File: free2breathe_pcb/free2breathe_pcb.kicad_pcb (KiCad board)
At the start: 2 copper layers, 108.5 x 115 mm, 102 parts, among them J1 USB4110-GF-A_REVB, J2 LED_Connector, J3 Alarm_Connector, Q1 AO3401A, Q2 DMN3404L, U1 IP5328, U2 MCP6044-E/P, U3 MCP6044-E/P, U4 SO2 Sensor, U5 CO Sensor, U6 MCP6044-E/P, U7 O3 Sensor, U8 MCP6044-E/P, U9 NO2 Sensor

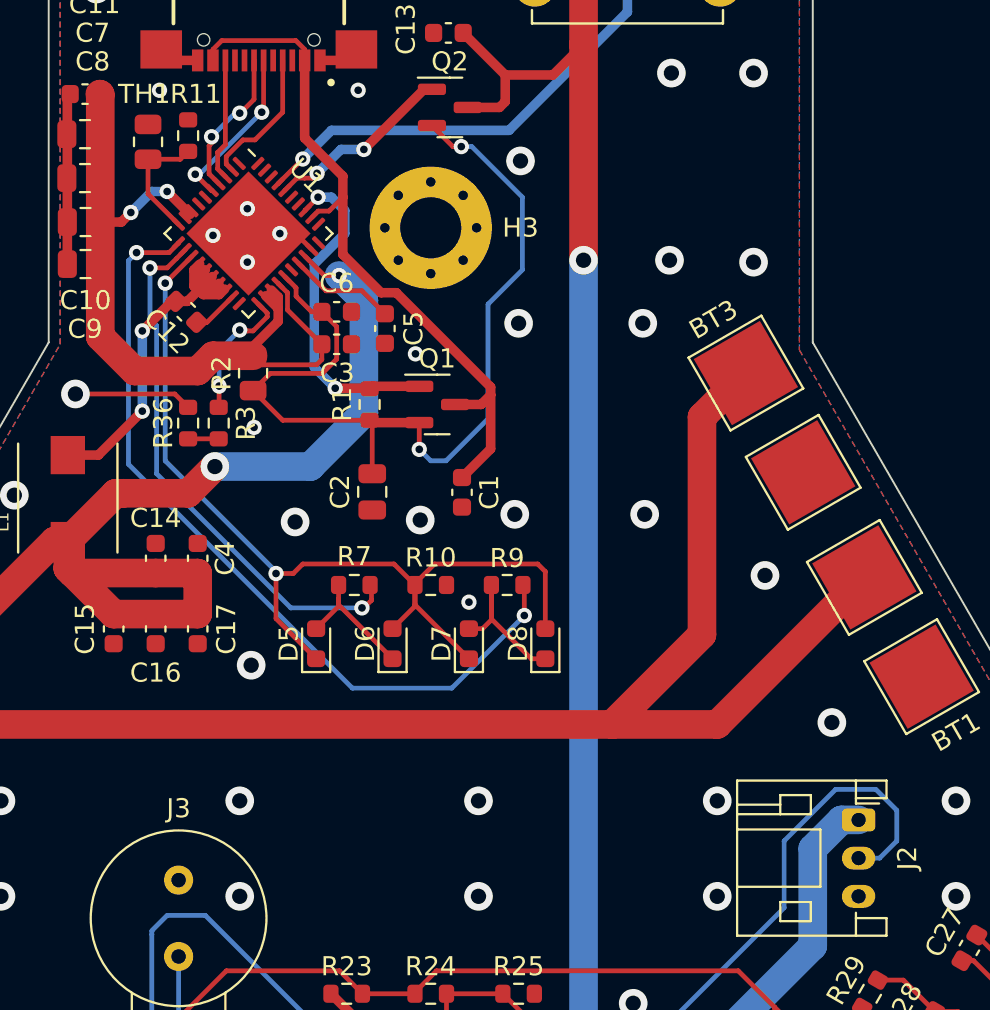
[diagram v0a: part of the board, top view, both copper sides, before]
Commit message: add fabrication files, update todo
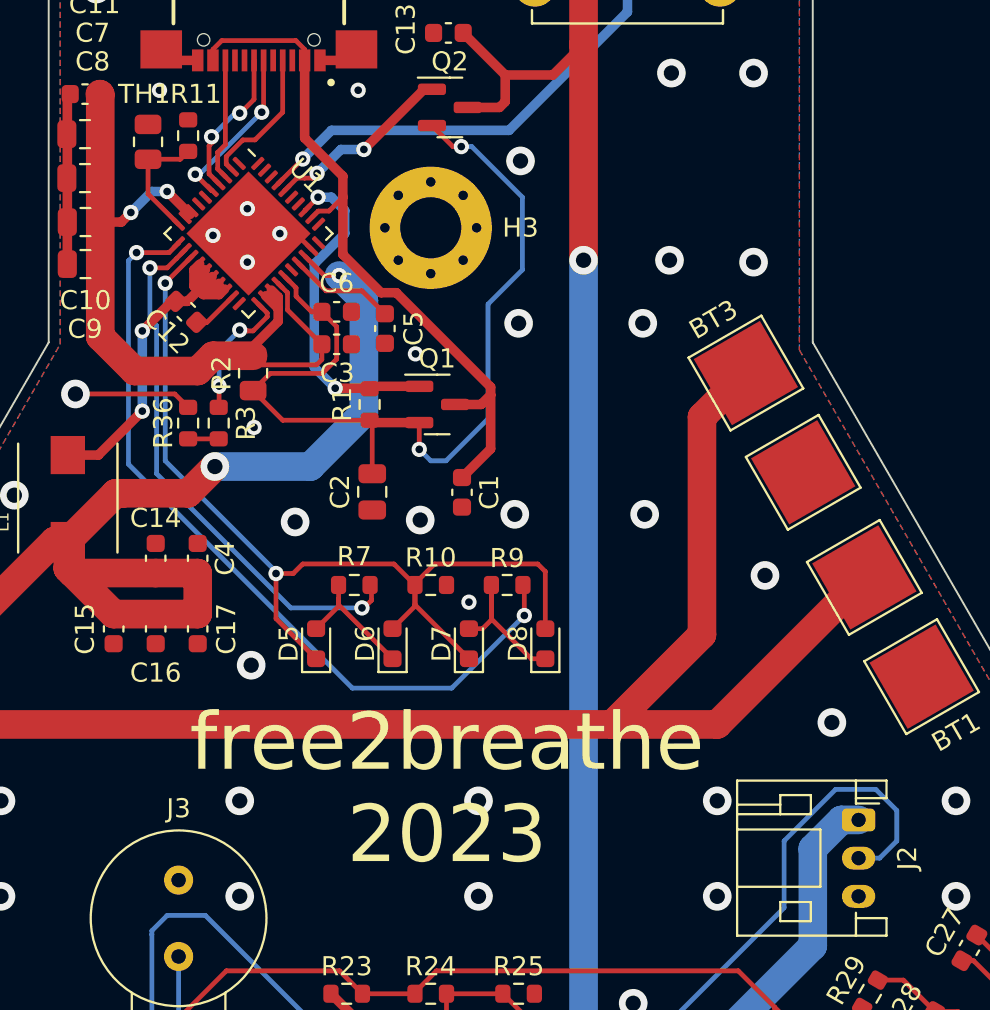
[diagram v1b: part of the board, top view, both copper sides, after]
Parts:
- added G***: LOGO, LOGO, B.Cu at (121.7, 92.5)
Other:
- board text added: "free2breathe 2023"

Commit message: start layout v2
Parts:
- added C33: 0.1u, Capacitor_SMD:C_0603_1608Metric, F.Cu at (196.1, 133.9)
- added R37: 49.9, Resistor_SMD:R_0603_1608Metric, F.Cu at (67.4, 161.8)
- added R38: 49.9, Resistor_SMD:R_0603_1608Metric, F.Cu at (190.3, 131.8)
- added R39: 100k, Resistor_SMD:R_0603_1608Metric, F.Cu at (81.4, 168.4)
- added R40: 499k, Resistor_SMD:R_0603_1608Metric, F.Cu at (193.1, 127.7)
- C15: value 22uF 16v -> 22uF 16V
- C18, C19, C24, C25: value 0.1u -> 1u
- R12: value 10 -> 2k
- R13: value 10k -> 1M
- R14, R16, R20, R21, R26, R28, R29, R31, R34, R35: value 10 -> 1M
- R15, R30: value 10 -> 16.2k
- R17: value 4.7k -> 1M
- R18, R19, R32, R33: value 10 -> 100K
- R22: value 10 -> 49.9
- R23: value 10k -> 49.9
- R24: value 910 -> 100k
- R25: value 4.7k -> 499k
- R27: value 10 -> 143k
- U4: value SO2 Sensor -> O3 Sensor
- U7: value O3 Sensor -> MCP6044-E/P; footprint components:XDCR_110-102 -> components:DIP254P762X533-14
- U8: value MCP6044-E/P -> SO2 Sensor; footprint components:DIP254P762X533-14 -> components:XDCR_110-102
- moved R19 107.4 mm to (183.7, 158.2), turned to 0 degrees
- moved C21 99.4 mm to (180.2, 163.9), turned to 0 degrees
- moved C28 98.0 mm to (67.6, 165.4), turned to 0 degrees
- moved R21 96.4 mm to (171.0, 159.8), turned to 0 degrees
- moved C23 95.9 mm to (166.5, 163.0), turned to 0 degrees
- moved R16 91.1 mm to (170.2, 155.9), turned to 0 degrees
- moved R27 90.1 mm to (73.8, 155.2), turned to 0 degrees
- moved R34 86.6 mm to (65.5, 157.8), turned to 0 degrees
- moved R23 83.4 mm to (173.8, 164.8)
- moved R14 79.7 mm to (162.7, 160.9), turned to 0 degrees
- moved R26 77.9 mm to (73.1, 151.4), turned to 0 degrees
- moved R25 75.8 mm to (178.0, 158.9)
- moved C24 74.7 mm to (175.3, 156.3), turned to 0 degrees
- moved C31 74.0 mm to (68.0, 110.1), turned to 0 degrees
- moved C26 73.2 mm to (72.2, 169.2), turned to 0 degrees
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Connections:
- A1 pad 23: /Arduino_A4 -> unconnected-(A1-Pad23)
- A1 pad 24: /Arduino_A5 -> unconnected-(A1-Pad24)
- A1 pad 25: /Arduino_A6 -> unconnected-(A1-Pad25)
- A1 pad 26: /Arduino_A7 -> unconnected-(A1-Pad26)
- C18 pad 1: Net-(C18-Pad1) -> Net-(R34-Pad2)
- C18 pad 2: Net-(C18-Pad2) -> GND
- C19 pad 1: Net-(C19-Pad1) -> Net-(R20-Pad2)
- C19 pad 2: Net-(C19-Pad2) -> GND
- C20 pad 2: GND -> Net-(C20-Pad2)
- C21 pad 2: GND -> Net-(C21-Pad2)
- C24 pad 1: Net-(C24-Pad1) -> Net-(R21-Pad2)
- C25 pad 1: Net-(C25-Pad1) -> Net-(R35-Pad2)
- C25 pad 2: Net-(C25-Pad2) -> GND
- C26 pad 2: GND -> Net-(C26-Pad2)
- C28 pad 2: GND -> Net-(C28-Pad2)
- C30 pad 1: Net-(C30-Pad1) -> Net-(R32-Pad2)
- C31 pad 1: Net-(C31-Pad1) -> Net-(R18-Pad2)
- C31 pad 2: Net-(C31-Pad2) -> GND
- C32 pad 1: Net-(C32-Pad1) -> Net-(R19-Pad2)
- R12 pad 1: Net-(C18-Pad1) -> Net-(R12-Pad1)
- R13 pad 2: /1.024V -> Net-(R12-Pad1)
- R14 pad 1: Net-(C19-Pad1) -> /Arduino_3V3
- R15 pad 1: /Divider_Low -> Net-(R14-Pad2)
- R15 pad 2: Net-(C20-Pad1) -> Net-(R15-Pad2)
- R16 pad 1: /1.024V -> Net-(R15-Pad2)
- R16 pad 2: Net-(C21-Pad1) -> GND
- R17 pad 1: /1.024V -> Net-(R12-Pad2)
- R18 pad 1: Net-(R18-Pad1) -> Net-(C20-Pad2)
- R18 pad 2: Net-(C22-Pad2) -> Net-(R18-Pad2)
- R19 pad 1: Net-(R19-Pad1) -> Net-(C21-Pad2)
- R19 pad 2: Net-(C23-Pad2) -> Net-(R19-Pad2)
- R20 pad 1: Net-(C22-Pad2) -> Net-(R20-Pad1)
- R20 pad 2: Net-(C22-Pad1) -> Net-(R20-Pad2)
- R21 pad 1: Net-(C23-Pad2) -> Net-(R21-Pad1)
- R21 pad 2: Net-(C23-Pad1) -> Net-(R21-Pad2)
- R22 pad 1: /Divider_High -> Net-(R22-Pad1)
- R22 pad 2: Net-(C24-Pad1) -> Net-(C22-Pad2)
- R23 pad 1: /Arduino_3V3 -> Net-(R23-Pad1)
- R23 pad 2: /Divider_High -> Net-(C23-Pad2)
- R24 pad 1: /Divider_High -> Net-(C20-Pad2)
- R24 pad 2: /Divider_Low -> Net-(C20-Pad1)
- R25 pad 1: /Divider_Low -> Net-(C21-Pad2)
- R25 pad 2: GND -> Net-(C21-Pad1)
- R26 pad 1: Net-(C25-Pad1) -> /Arduino_3V3
- R27 pad 1: Net-(C27-Pad1) -> Net-(R26-Pad2)
- R28 pad 1: /Divider_High -> Net-(R27-Pad2)
- R28 pad 2: Net-(C26-Pad1) -> GND
- R29 pad 1: /Divider_High -> /Arduino_3V3
- R29 pad 2: Net-(C28-Pad1) -> Net-(R29-Pad2)
- R30 pad 1: Net-(R30-Pad1) -> Net-(R29-Pad2)
- R30 pad 2: Net-(C29-Pad2) -> Net-(R30-Pad2)
- R31 pad 1: Net-(R31-Pad1) -> Net-(R30-Pad2)
- R31 pad 2: Net-(C31-Pad2) -> GND
- R32 pad 1: Net-(C29-Pad2) -> Net-(C26-Pad2)
- R32 pad 2: Net-(C29-Pad1) -> Net-(R32-Pad2)
- R33 pad 1: /Divider_Low -> Net-(C27-Pad2)
- R33 pad 2: Net-(C30-Pad1) -> Net-(R33-Pad2)
- R34 pad 1: Net-(C31-Pad2) -> Net-(R34-Pad1)
- R34 pad 2: Net-(C31-Pad1) -> Net-(R34-Pad2)
- R35 pad 1: /Divider_Low -> Net-(R35-Pad1)
- R35 pad 2: Net-(C32-Pad1) -> Net-(R35-Pad2)
- U2 pad 1: Net-(C18-Pad1) -> Net-(R21-Pad1)
- U2 pad 10: Net-(C22-Pad2) -> Net-(R14-Pad2)
- U2 pad 12: Net-(C22-Pad1) -> Net-(R19-Pad2)
- U2 pad 2: Net-(C18-Pad2) -> Net-(C23-Pad1)
- U2 pad 3: Net-(C20-Pad1) -> Net-(R15-Pad2)
- U2 pad 5: Net-(C24-Pad1) -> Net-(R21-Pad2)
- U2 pad 6: Net-(C22-Pad2) -> Net-(R23-Pad1)
- U2 pad 7: Net-(C22-Pad1) -> Net-(R23-Pad1)
- U2 pad 8: /Arduino_A3 -> Net-(C21-Pad2)
- U2 pad 9: /Arduino_A3 -> Net-(C21-Pad1)
- U3 pad 1: Net-(C19-Pad1) -> Net-(R20-Pad1)
- U3 pad 10: Net-(C23-Pad2) -> Net-(R12-Pad2)
- U3 pad 12: Net-(C23-Pad1) -> Net-(R18-Pad2)
- U3 pad 2: Net-(C19-Pad2) -> Net-(C22-Pad1)
- U3 pad 3: Net-(C21-Pad1) -> Net-(R12-Pad1)
- U3 pad 5: Net-(C21-Pad1) -> Net-(R20-Pad2)
- U3 pad 6: Net-(C23-Pad2) -> Net-(R22-Pad1)
- U3 pad 7: Net-(C23-Pad1) -> Net-(R22-Pad1)
- U3 pad 8: /Arduino_A1 -> Net-(C20-Pad2)
- U3 pad 9: /Arduino_A1 -> Net-(C20-Pad1)
- U4 pad 1: Net-(R18-Pad1) -> Net-(C21-Pad1)
- U4 pad 4: Net-(C18-Pad2) -> Net-(C23-Pad1)
- U4 pad 5: Net-(R12-Pad2) -> Net-(C23-Pad2)
- U4 pad 6: Net-(R18-Pad1) -> Net-(C21-Pad1)
- U5 pad 1: Net-(R19-Pad1) -> Net-(C20-Pad1)
- U5 pad 4: Net-(C19-Pad2) -> Net-(C22-Pad1)
- U5 pad 5: Net-(R14-Pad2) -> Net-(C22-Pad2)
- U5 pad 6: Net-(R19-Pad1) -> Net-(C20-Pad1)
- U6 pad 1: Net-(C25-Pad1) -> Net-(R34-Pad1)
- U6 pad 10: Net-(C29-Pad2) -> Net-(R27-Pad2)
- U6 pad 12: Net-(C29-Pad1) -> Net-(R32-Pad2)
- U6 pad 13: /Arduino_A4 -> /Arduino_A1
- U6 pad 14: /Arduino_A4 -> /Arduino_A1
- U6 pad 2: Net-(C25-Pad2) -> Net-(C28-Pad1)
- U6 pad 3: Net-(C26-Pad1) -> Net-(R26-Pad2)
- U6 pad 5: Net-(C30-Pad1) -> Net-(R34-Pad2)
- U6 pad 6: Net-(C29-Pad2) -> Net-(R37-Pad1)
- U6 pad 7: Net-(C29-Pad1) -> Net-(R37-Pad1)
- U6 pad 8: /Arduino_A5 -> Net-(C26-Pad2)
- U6 pad 9: /Arduino_A5 -> Net-(C26-Pad1)
- U7 pad 1: Net-(R30-Pad1) -> Net-(R35-Pad1)
- U7 pad 2: unconnected-(U7-Pad2) -> Net-(C29-Pad1)
- U7 pad 3: unconnected-(U7-Pad3) -> Net-(R30-Pad2)
- U7 pad 4: Net-(C25-Pad2) -> /Arduino_3V3
- U7 pad 5: Net-(R26-Pad2) -> Net-(R35-Pad2)
- U7 pad 6: Net-(R30-Pad1) -> Net-(R38-Pad1)
- U8 pad 1: Net-(C27-Pad1) -> Net-(C26-Pad1)
- U8 pad 2: Net-(C27-Pad2) -> unconnected-(U8-Pad2)
- U8 pad 3: Net-(C28-Pad1) -> unconnected-(U8-Pad3)
- U8 pad 4: /Arduino_3V3 -> Net-(C28-Pad1)
- U8 pad 5: Net-(C32-Pad1) -> Net-(C28-Pad2)
- U8 pad 6: Net-(C31-Pad2) -> Net-(C26-Pad1)
- U9 pad 1: Net-(R31-Pad1) -> Net-(C27-Pad1)
- U9 pad 4: Net-(C27-Pad2) -> Net-(C29-Pad1)
- U9 pad 5: Net-(R27-Pad2) -> Net-(C29-Pad2)
- U9 pad 6: Net-(R31-Pad1) -> Net-(C27-Pad1)
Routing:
- net /Arduino_3V3: track 156.7 -> 0.00 mm, vias 6 -> 0
- net /Arduino_A1: track 125.3 -> 0.00 mm, vias 2 -> 0
- net /Arduino_A0: track 104.9 -> 0.00 mm
- net /Divider_Low: track 98.5 -> 0.00 mm, vias 4 -> 0
- net /Divider_High: track 85.8 -> 0.00 mm, vias 2 -> 0
- net /Arduino_D8: track 76.5 -> 0.00 mm, vias 2 -> 0
- net /Arduino_A3: track 76.0 -> 0.00 mm, vias 2 -> 0
- net /Arduino_A2: track 73.1 -> 0.00 mm
- net /Arduino_D13: track 64.1 -> 0.00 mm
- net /Arduino_D12: track 48.9 -> 0.00 mm
- net /Arduino_D9: track 48.9 -> 0.00 mm
- net /Arduino_D10: track 44.9 -> 0.00 mm
- net /Arduino_A6: track 43.3 -> 0.00 mm, vias 2 -> 0
- net /Arduino_D11: track 39.8 -> 0.00 mm
- net Net-(C27-Pad2): track 33.0 -> 0.00 mm
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- removed copper zone on F.Cu, net GND

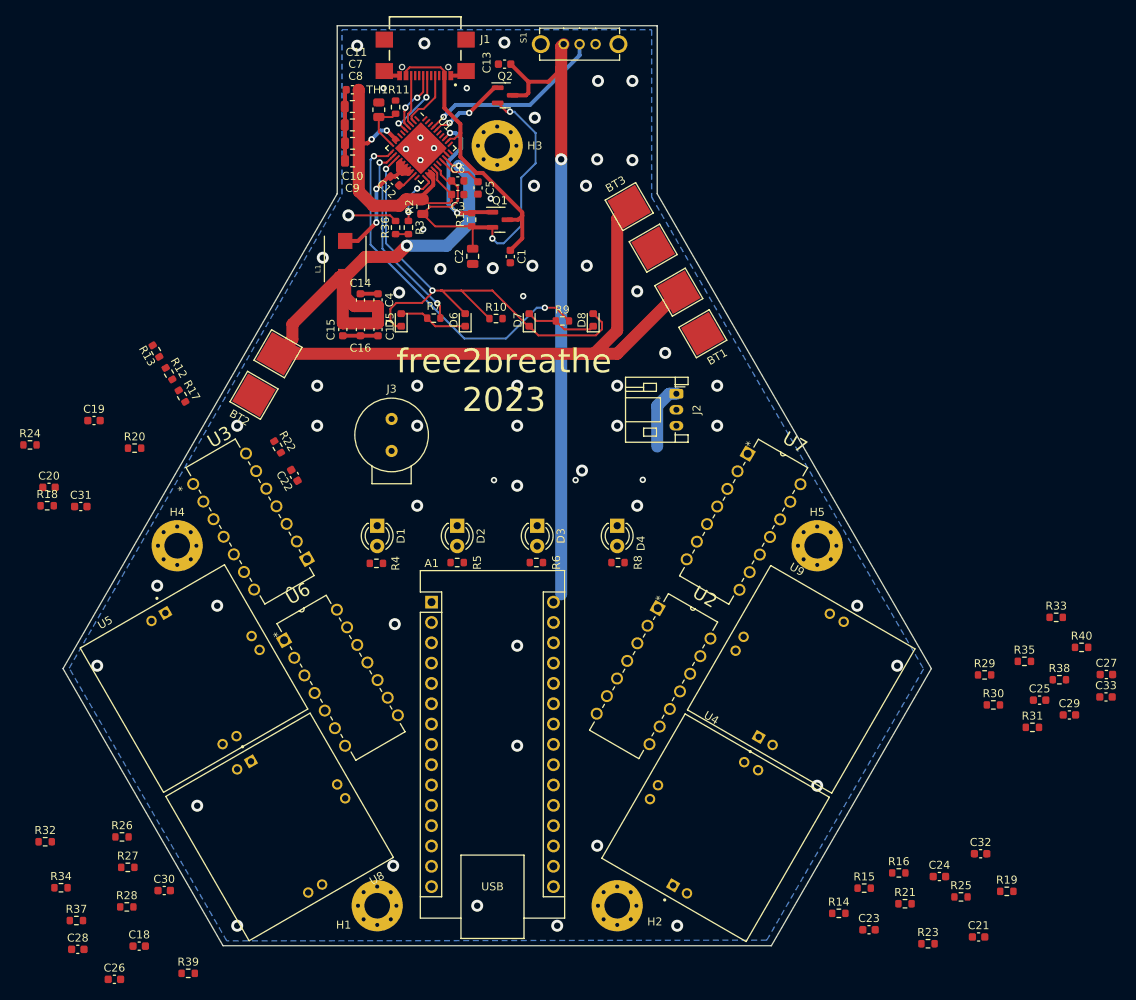
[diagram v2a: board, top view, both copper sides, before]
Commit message: changed LED resistors, placed rev2 components
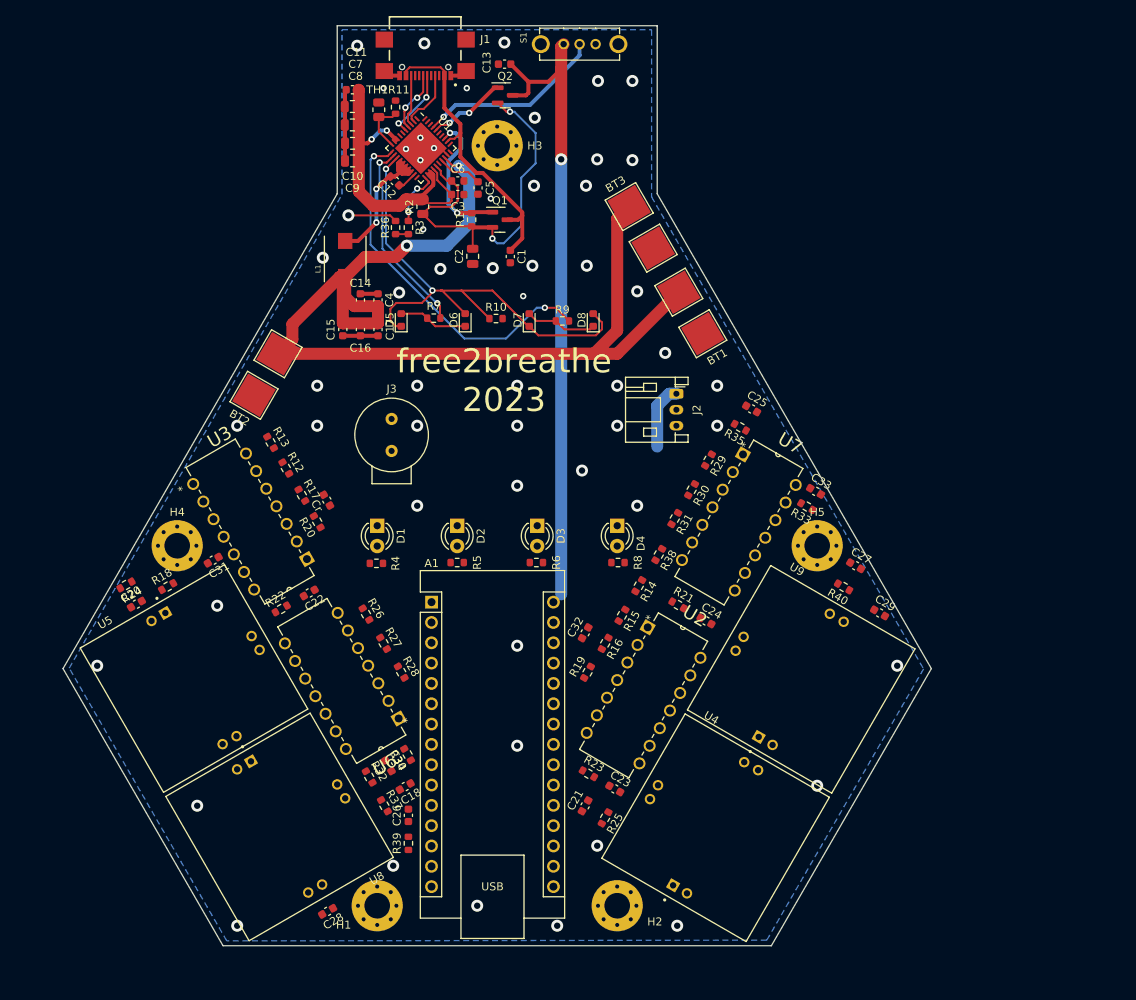
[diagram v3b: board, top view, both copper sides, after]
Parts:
- moved R19 59.1 mm to (131.3, 130.8), turned to 60 degrees
- moved C32 56.6 mm to (131.0, 125.9), turned to 60 degrees
- moved R38 52.5 mm to (140.2, 116.1), turned to -120 degrees
- moved C21 51.8 mm to (131.0, 147.5), turned to 60 degrees
- moved R31 51.8 mm to (142.2, 111.6), turned to -120 degrees
- moved C25 51.2 mm to (151.8, 97.9), turned to -30 degrees
- moved R14 48.0 mm to (137.7, 120.0), turned to -120 degrees
- moved R23 47.5 mm to (131.4, 143.5), turned to -30 degrees
- moved R21 46.9 mm to (142.6, 122.4), turned to -30 degrees
- moved R16 46.6 mm to (133.5, 127.2), turned to -120 degrees
- moved R34 46.4 mm to (108.8, 141.1), turned to 120 degrees
- moved R30 46.3 mm to (144.3, 108.0), turned to -120 degrees
- moved R35 46.0 mm to (150.4, 100.2), turned to 150 degrees
- moved R15 45.6 mm to (135.6, 123.7), turned to -120 degrees
- moved R25 45.6 mm to (133.5, 149.0), turned to -120 degrees
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- renumbered C19 to Cr
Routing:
- net GND: vias 59 -> 56
- net (no net): vias 3 -> 0

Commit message: completed rev2
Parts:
- added G***: LOGO, components:free2breathe, F.Cu at (122.2, 95.8)
- R4, R5, R6, R8: value R -> 220
- moved R23 1.01 mm to (132.3, 144.0)
- moved C23 0.81 mm to (135.4, 145.8), turned to 60 degrees
- moved C31 0.10 mm to (84.6, 116.8)
- turned C33 to 150 degrees
- renumbered Cr to C19
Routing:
- net /Arduino_3V3: track 0.00 -> 134.8 mm, vias 0 -> 2
- net /Arduino_D8: track 0.00 -> 65.3 mm, vias 0 -> 1
- net /Arduino_A0: track 0.00 -> 58.6 mm, vias 0 -> 1
- net /Arduino_A3: track 0.00 -> 53.6 mm, vias 0 -> 2
- net /Arduino_D13: track 0.00 -> 53.0 mm
- net /Arduino_D9: track 0.00 -> 52.4 mm
- net /Arduino_D12: track 0.00 -> 45.6 mm
- net /Arduino_D10: track 0.00 -> 44.2 mm
- net Net-(C26-Pad1): track 0.00 -> 43.7 mm, vias 0 -> 1
- net /Arduino_D11: track 0.00 -> 40.4 mm
- net Net-(C27-Pad1): track 0.00 -> 39.8 mm
- net Net-(C23-Pad1): track 0.00 -> 39.3 mm, vias 0 -> 1
- net Net-(C26-Pad2): track 0.00 -> 37.6 mm
- net Net-(C22-Pad2): track 0.00 -> 34.3 mm
- net Net-(C22-Pad1): track 0.00 -> 34.0 mm
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- added copper zone on F.Cu, net GND
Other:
- board text added: "2023 Rev. 2"
- board text removed: "free2breathe 2023"
